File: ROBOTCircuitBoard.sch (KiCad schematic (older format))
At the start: 20 parts, among them J1 DB15_HighDensity_MountingHoles, J2 DB15_HighDensity_MountingHoles, P1 CONN_01X03, P13 CONN_01X04, P15 CONN_01X04, P2 CONN_01X04, P24 CONN_01X04, P3 CONN_01X04, P4 CONN_01X04, P5 CONN_01X05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

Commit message: Connected main chip and bootloader
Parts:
- removed D1, D2: LED, LEDs:LED_0805, symbol LED
- removed P13, P15, P24, P3, P4, P6, P7, P8: CONN_01X04, Socket_Strips:Socket_Strip_Straight_1x04_Pitch2.54mm, symbol CONN_01X04
- removed R1, R2: R, Resistors_THT:R_Box_L8.4mm_W2.5mm_P5.08mm, symbol R
- removed U2: Teensy3.2, Teensy:Teensy30_31_32_LC_LessPins, symbol Teensy3.2
- added P?: USB_B, symbol USB_B
- added P?: CONN_01X04, symbol CONN_01X04
- added P?: CONN_01X02, symbol CONN_01X02
- added U?: MK20DX256VLH7, QFP50P1200X1200X160-64N, symbol MK20DX256VLH7
- added U?: MKL02, symbol MKL02
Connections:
- net labels added: +3.3V, C0, C1, C2, C3, RESET
- net labels removed: 0A, 0B, 1A, 1B, A0, A1, A2, A3, A4, A5, A6, A7, A8, A9
- wire segments 56 -> 18
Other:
- moved on the sheet: C1, J1, J2, P1, P2, P5, U1

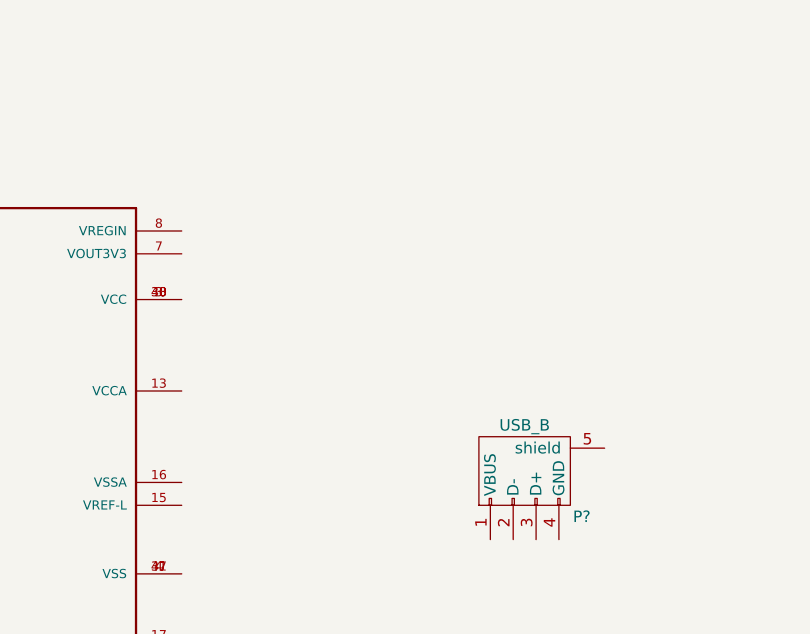
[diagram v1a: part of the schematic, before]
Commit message: Added reference folder with images
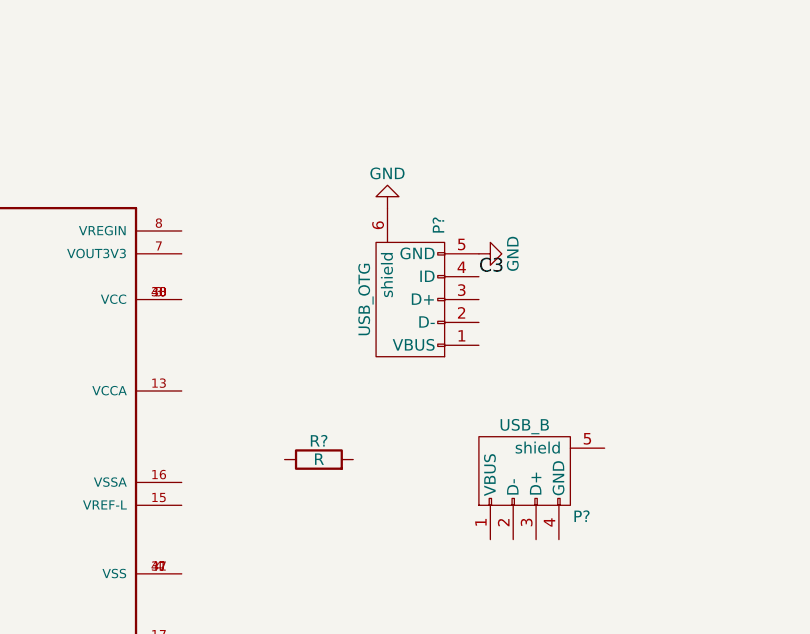
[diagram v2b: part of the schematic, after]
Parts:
- added P?: USB_OTG, symbol USB_OTG
- added R?: R, symbol R
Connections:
- net C3: now also P?.4 (ID)
- net GND: now also P?.5 (GND), P?.6 (shield)
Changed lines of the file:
@@
 LIBS:contrib
 LIBS:valves
-LIBS:MK20DX256VLH7
+LIBS:ROBOTCircuitBoard-cache
 EELAYER 25 0
 EELAYER END
@@
 Text Label 3650 6250 0    60   ~ 0
 RESET
+$Comp
+L USB_OTG P?
+U 1 1 58D99EF8
+P 4650 3750
+F 0 "P?" H 4975 3625 50  0000 C CNN
+F 1 "USB_OTG" H 4650 3950 50  0000 C CNN
+F 2 "" V 4600 3650 50  0000 C CNN
+F 3 "" V 4600 3650 50  0000 C CNN
+	1    4650 3750
+	0    -1   -1   0
+$EndComp
+Text Label 4950 3650 0    60   ~ 0
+C3
+$Comp
+L GND #PWR?
+U 1 1 58D99FDB
+P 4950 3550
+F 0 "#PWR?" H 4950 3300 50  0001 C CNN
+F 1 "GND" H 4950 3400 50  0000 C CNN
+F 2 "" H 4950 3550 50  0000 C CNN
+F 3 "" H 4950 3550 50  0000 C CNN
+	1    4950 3550
+	0    -1   -1   0
+$EndComp
+$Comp
+L GND #PWR?
+U 1 1 58D9A00D
+P 4550 3350
+F 0 "#PWR?" H 4550 3100 50  0001 C CNN
+F 1 "GND" H 4550 3200 50  0000 C CNN
+F 2 "" H 4550 3350 50  0000 C CNN
+F 3 "" H 4550 3350 50  0000 C CNN
+	1    4550 3350
+	-1   0    0    1
+$EndComp
+$Comp
+L R R?
+U 1 1 58D9A0F7
+P 4250 4450
+F 0 "R?" V 4330 4450 50  0000 C CNN
+F 1 "R" V 4250 4450 50  0000 C CNN
+F 2 "" V 4180 4450 50  0000 C CNN
+F 3 "" H 4250 4450 50  0000 C CNN
+	1    4250 4450
+	0    -1   -1   0
+$EndComp
 $EndSCHEMATC

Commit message: worked more on the teensy
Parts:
- removed P?: USB_B, symbol USB_B
- added C?: CP1, symbol CP1
- added L?: L, symbol L
- added R?: R, symbol R
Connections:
- net labels added: M, P
- wire segments 18 -> 27
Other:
- note added: "D0 – D33 are the Digital Ports\n"
- note added: "Find Inductor\n"
- moved on the sheet: R?
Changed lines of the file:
@@
-$EndComp
-$Comp
-L USB_B P?
-U 1 1 58D82827
-P 5200 4500
-F 0 "P?" H 5400 4300 50  0000 C CNN
-F 1 "USB_B" H 5150 4700 50  0000 C CNN
-F 2 "" V 5150 4400 50  0000 C CNN
-F 3 "" V 5150 4400 50  0000 C CNN
-	1    5200 4500
-	1    0    0    -1
 $EndComp
 $Comp
@@
 L R R?
 U 1 1 58D9A0F7
-P 4250 4450
-F 0 "R?" V 4330 4450 50  0000 C CNN
-F 1 "R" V 4250 4450 50  0000 C CNN
-F 2 "" V 4180 4450 50  0000 C CNN
-F 3 "" H 4250 4450 50  0000 C CNN
-	1    4250 4450
-	0    -1   -1   0
-$EndComp
+P 3800 7450
+F 0 "R?" V 3880 7450 50  0000 C CNN
+F 1 "R" V 3800 7450 50  0000 C CNN
+F 2 "" V 3730 7450 50  0000 C CNN
+F 3 "" H 3800 7450 50  0000 C CNN
+	1    3800 7450
+	0    -1   -1   0
+$EndComp
+Text Notes -150 3700 0    60   ~ 0
+D0 – D33 are the Digital Ports\n
+$Comp
+L GND #PWR?
+U 1 1 5932029C
+P 3650 4950
+F 0 "#PWR?" H 3650 4700 50  0001 C CNN
+F 1 "GND" H 3650 4800 50  0000 C CNN
+F 2 "" H 3650 4950 50  0000 C CNN
+F 3 "" H 3650 4950 50  0000 C CNN
+	1    3650 4950
+	0    -1   -1   0
+$EndComp
+Text Notes 5450 2950 0    60   ~ 0
+Find Inductor\n
+Wire Wire Line
+	3650 4550 3650 4650
+$Comp
+L CP1 C?
+U 1 1 593205D8
+P 4050 4900
+F 0 "C?" H 4075 5000 50  0000 L CNN
+F 1 "CP1" H 4075 4800 50  0000 L CNN
+F 2 "" H 4050 4900 50  0000 C CNN
+F 3 "" H 4050 4900 50  0000 C CNN
+	1    4050 4900
+	-1   0    0    1
+$EndComp
+Wire Wire Line
+	3650 4650 4050 4650
+Wire Wire Line
+	4050 4650 4050 4750
+Wire Wire Line
+	4050 5050 4050 5250
+Wire Wire Line
+	4050 5250 3650 5250
+$Comp
+L L L?
+U 1 1 5932084F
+P 4200 4650
+F 0 "L?" V 4150 4650 50  0000 C CNN
+F 1 "L" V 4275 4650 50  0000 C CNN
+F 2 "" H 4200 4650 50  0000 C CNN
+F 3 "" H 4200 4650 50  0000 C CNN
+	1    4200 4650
+	0    -1   -1   0
+$EndComp
+$Comp
+L GND #PWR?
+U 1 1 59320A11
+P 4350 4650
+F 0 "#PWR?" H 4350 4400 50  0001 C CNN
+F 1 "GND" H 4350 4500 50  0000 C CNN
+F 2 "" H 4350 4650 50  0000 C CNN
+F 3 "" H 4350 4650 50  0000 C CNN
+	1    4350 4650
+	0    -1   -1   0
+$EndComp
+Wire Wire Line
+	3950 7450 4250 7450
+Connection ~ 4100 7450
+Text Label 4950 3750 0    60   ~ 0
+M
+Text Label 4950 3850 0    60   ~ 0
+P
+Text Label 4250 7450 0    60   ~ 0
+M
+$Comp
+L R R?
+U 1 1 59320DBD
+P 3800 7350
+F 0 "R?" V 3880 7350 50  0000 C CNN
+F 1 "R" V 3800 7350 50  0000 C CNN
+F 2 "" V 3730 7350 50  0000 C CNN
+F 3 "" H 3800 7350 50  0000 C CNN
+	1    3800 7350
+	0    -1   -1   0
+$EndComp
+Wire Wire Line
+	3950 7350 4250 7350
+Wire Wire Line
+	4100 7350 4100 7200
+Connection ~ 4100 7350
+Wire Wire Line
+	4100 7450 4100 7600
+Text Label 4250 7350 0    60   ~ 0
+P
 $EndSCHEMATC

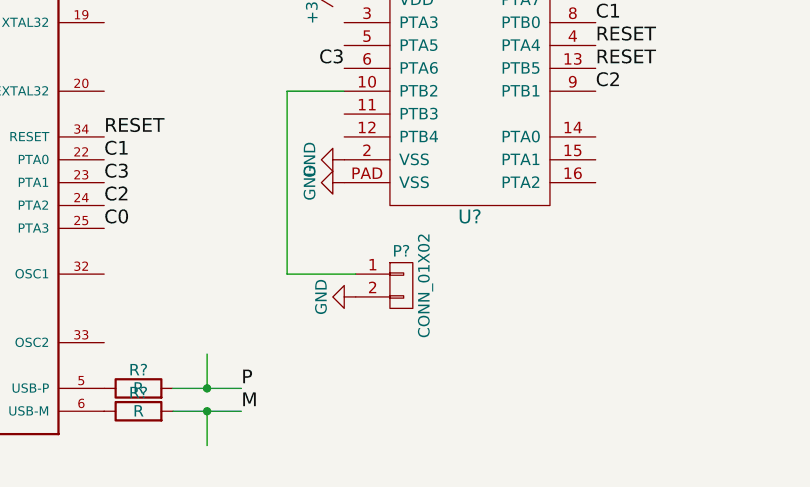
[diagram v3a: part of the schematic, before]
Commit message: Labled a button
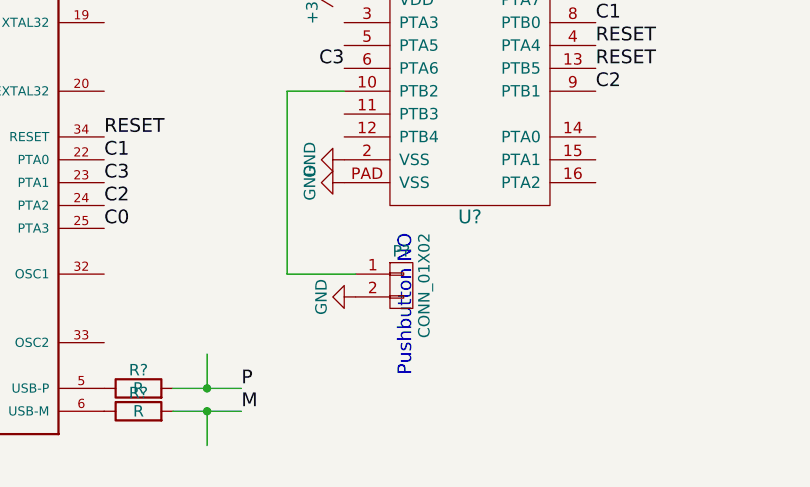
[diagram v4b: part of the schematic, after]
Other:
- note added: "Pushbutton NO\n"
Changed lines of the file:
@@
 Text Label 4250 7350 0    60   ~ 0
 P
+Text Notes 5000 7300 1    60   ~ 0
+Pushbutton NO\n
 $EndSCHEMATC
